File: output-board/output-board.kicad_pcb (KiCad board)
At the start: 2 copper layers, 121.9 x 86 mm, 98 parts, among them P1 CONN_2, P2 CONN_01X09, Q1 NPN, Q2 NPN, Q3 NPN, Q4 NPN, Q5 NPN, Q6 NPN, Q7 NPN, Q8 NPN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

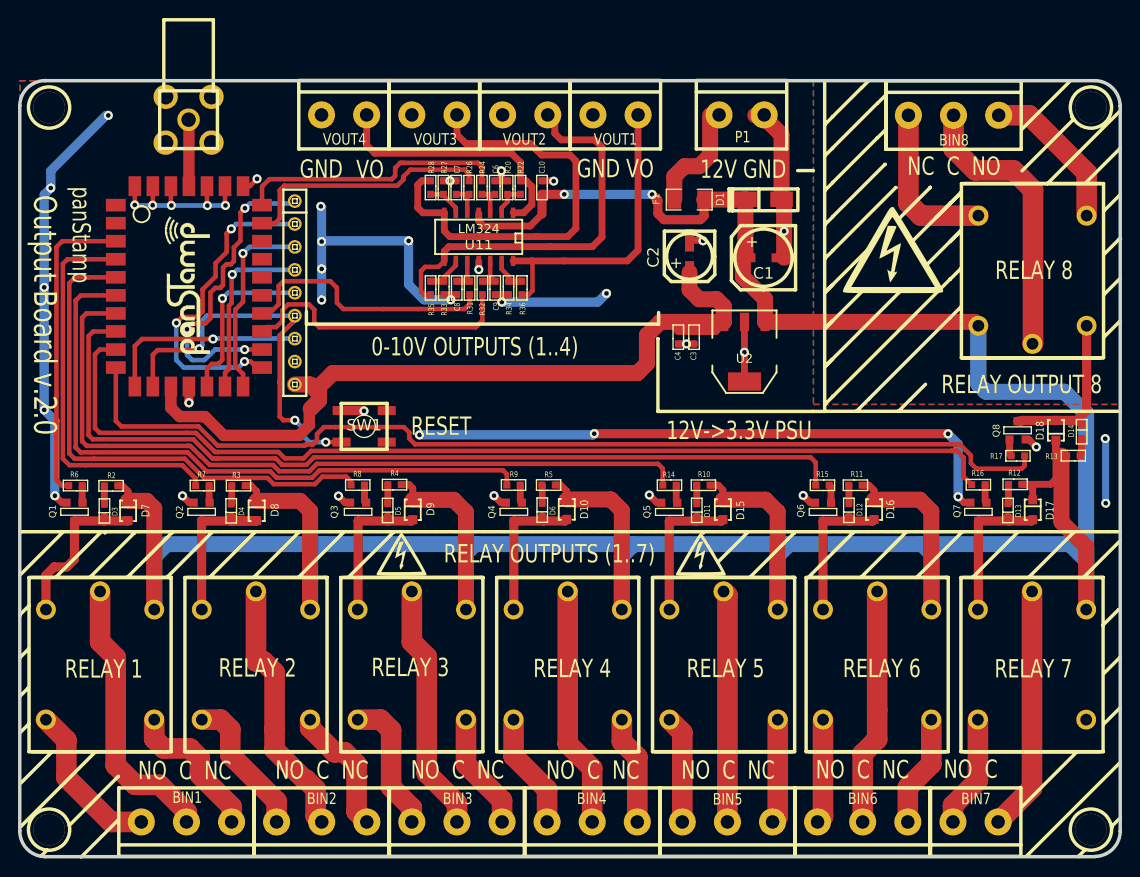
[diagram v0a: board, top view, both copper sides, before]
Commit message: Fiducials added to the PCB
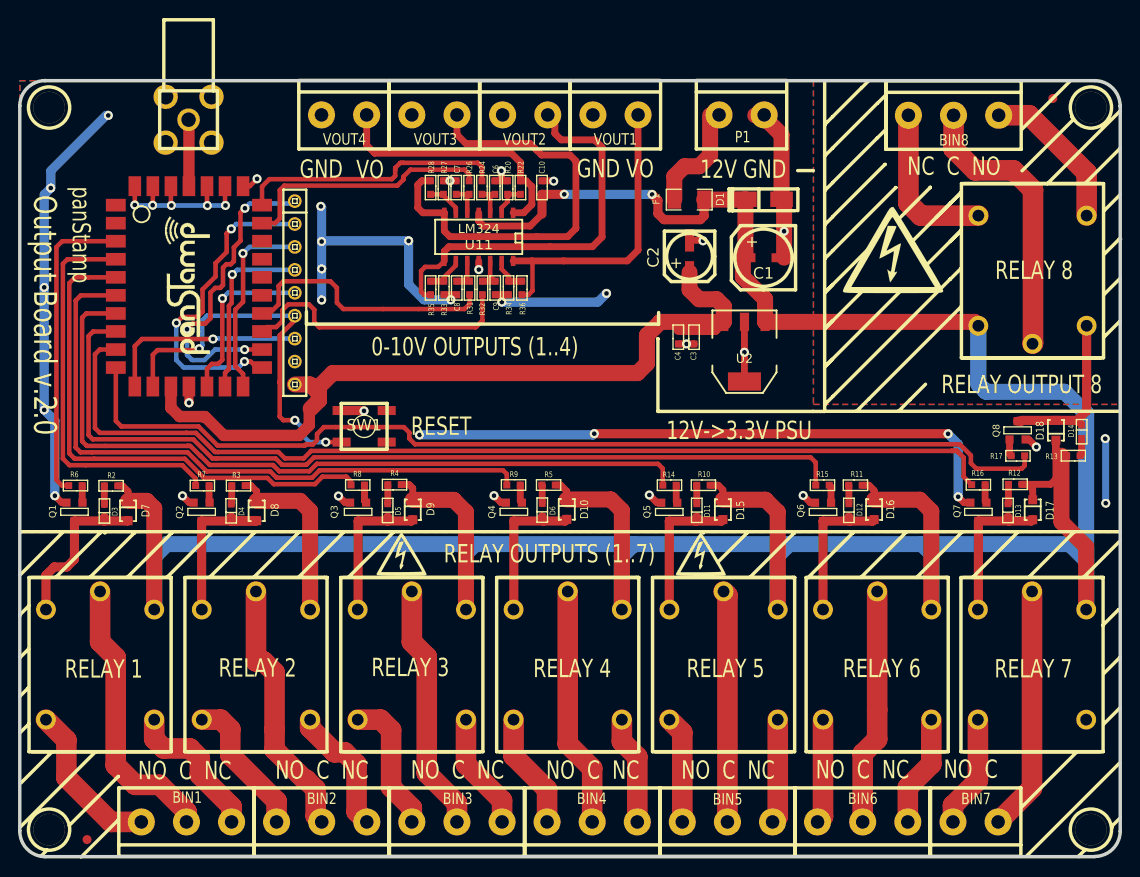
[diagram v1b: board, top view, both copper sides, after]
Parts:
- added fiducial: VAL**, mymods:fiducial, F.Cu at (142.8, 127.0)
- added fiducial: VAL**, mymods:fiducial, F.Cu at (249.8, 44.8)
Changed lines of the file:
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@@
-(kicad_pcb (version 4) (host pcbnew "(2014-jul-16 BZR unknown)-product")
+(kicad_pcb (version 4) (host pcbnew no-vcs-found-product)
   (general
     (links 185)
     (no_connects 0)
-    (area 135.181339 42.664265 257.502661 129.044701)
+    (area 122.186699 35.725099 259.600701 133.5324)
     (thickness 1.6002)
     (drawings 207)
     (tracks 845)
     (zones 0)
-    (modules 98)
+    (modules 100)
     (nets 91)
   )
@@
   )
   (setup
-    (last_trace_width 0.508)
+    (last_trace_width 0.254)
     (user_trace_width 0.254)
     (user_trace_width 0.381)
@@
     (pad_to_mask_clearance 0.254)
     (aux_axis_origin 0 0)
-    (visible_elements FFFFF77F)
+    (visible_elements FFFFF7FF)
     (pcbplotparams
-      (layerselection 0x00020_80000001)
+      (layerselection 0x010e0_80000001)
       (usegerberextensions true)
       (excludeedgelayer true)
@@
       (drillshape 0)
       (scaleselection 1)
-      (outputdirectory /home/daniel/development/kicad/panstamp/current/output-board/production/))
+      (outputdirectory production/))
   )
   (net 0 "")
@@
       (net 2 +3.3V))
   )
+  (module mymods:fiducial (layer Front)
+    (at 142.83 126.96)
+    (fp_text reference fiducial (at -1.75 5.15) (layer F.SilkS) hide
+      (effects (font (thickness 0.3048)))
+    )
+    (fp_text value VAL** (at -0.77 3.19) (layer F.SilkS) hide
+      (effects (font (thickness 0.3048)))
+    )
+    (pad 1 smd circle (at 0 0) (size 1 1) (layers Front F.Mask)
+      (solder_mask_margin 0.5) (clearance 0.5))
+  )
+  (module mymods:fiducial (layer Front)
+    (at 249.84 44.84)
+    (fp_text reference fiducial (at 0.08 -3.41) (layer F.SilkS) hide
+      (effects (font (thickness 0.3048)))
+    )
+    (fp_text value VAL** (at -0.36 -5.28) (layer F.SilkS) hide
+      (effects (font (thickness 0.3048)))
+    )
+    (pad 1 smd circle (at 0 0) (size 1 1) (layers Front F.Mask)
+      (solder_mask_margin 0.5) (clearance 0.5))
+  )
   (gr_line (start 216.00668 92.9386) (end 216.00668 92.92844) (angle 90) (layer F.SilkS) (width 0.381))
